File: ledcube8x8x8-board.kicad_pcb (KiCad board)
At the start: 4 copper layers, 120 x 90 mm, 219 parts, among them J1 282836-2, J10 molex_53261-0871, J11 104031-0811, J12 30306-6002HB, J13 hedear, J14 hedear, J15 30306-6002HB, J16 61201021621, J2 molex_53261-0871, J3 molex_53261-0871, J4 molex_53261-0871, J5 molex_53261-0871, J6 molex_53261-0871, J7 molex_53261-0871, J8 molex_53261-0871, J9 molex_53261-0871, Q1 Q_NMOS_GDSD, Q2 Q_NMOS_GDSD, Q3 Q_NMOS_GDSD, Q4 Q_NMOS_GDSD, Q5 Q_NMOS_GDSD, Q6 Q_NMOS_GDSD, Q7 Q_NMOS_GDSD, Q8 Q_NMOS_GDSD, Q9 Q_PMOS_GSD, U1 LM1085IS-12, U10 TL3305AF260QG, U11 IP4220CZ6, U12 IP4220CZ6, U13 XC9572XL-VQ64, U14 SN74LVCC3245APWR, U15 SN74LVCC3245APWR, U16 TS3A27518EPW, U2 STP08CP05MTR, U3 STP08CP05MTR, U4 STP08CP05MTR, U5 STP08CP05MTR, U6 STP08CP05MTR, U7 STP08CP05MTR, U8 STP08CP05MTR, U9 STP08CP05MTR, X1 ASE-40MHz, X2 ASE-25MHz

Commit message: Place whole PS part. Start with PL one.
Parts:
- removed C18, C19: 10nF, Capacitor_SMD:C_0805_2012Metric_Pad1.18x1.45mm_HandSolder
- removed X1: ASE-40MHz, Oscillator:Oscillator_SMD_Abracon_ASE-4Pin_3.2x2.5mm
- removed X2: ASE-25MHz, Oscillator:Oscillator_SMD_Abracon_ASE-4Pin_3.2x2.5mm
- added Q10: Q_PMOS_GSD, Package_TO_SOT_SMD:SOT-23, B.Cu at (52.8, 36.2)
- added R126: 10K, Resistor_SMD:R_0805_2012Metric_Pad1.20x1.40mm_HandSolder, B.Cu at (56.2, 36.2)
- C17, C32, C33, C34, D6, R1, R107, R112, R116, R119, R120, R121, R122, R2, R3, R81, R82, R85, R87, R92, R93, U14, U16: moved to B.Cu
- moved R6 240.0 mm to (153.8, 77.0), turned to 0 degrees
- moved R5 233.5 mm to (143.2, 83.5), turned to 0 degrees
- moved R8 230.9 mm to (153.8, 74.5), turned to 0 degrees
- moved R7 227.5 mm to (131.8, 83.8), turned to 0 degrees
- moved R10 221.8 mm to (153.8, 72.0), turned to 0 degrees
- moved R9 220.1 mm to (150.8, 63.8), turned to 0 degrees
- moved R12 212.7 mm to (153.8, 69.2), turned to 0 degrees
- moved C23 208.5 mm to (35.0, 57.2)
- moved R11 205.8 mm to (150.8, 61.0), turned to 0 degrees
- moved C24 201.3 mm to (30.2, 57.2), turned to 180 degrees
- moved U14 197.3 mm to (34.2, 56.8), turned to 270 degrees
- moved U15 196.9 mm to (33.0, 50.2), turned to 180 degrees
- moved R125 191.8 mm to (71.0, 68.2), turned to 90 degrees
- moved Q9 170.4 mm to (153.1, 44.7)
- moved R123 170.4 mm to (153.0, 40.8)
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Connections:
- C17 pad 1: Net-(C17-Pad1) -> /ps.sch/ESP_PU
- MOD1 pad 3: Net-(C17-Pad1) -> /ps.sch/ESP_PU
- R107 pad 2: Net-(C17-Pad1) -> /ps.sch/ESP_PU
- U16 pad 20: /power_supply.sch/~SYS_RST -> Net-(Q10-Pad3)
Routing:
- net ESP_3V3: track 0.00 -> 201.2 mm, vias 0 -> 8
- net GNDD: track 57.4 -> 128.6 mm
- net GND: track 56.6 -> 113.0 mm
- net /DATA_LED1: track 0.00 -> 55.5 mm, vias 0 -> 3
- net /ps.sch/TDI: track 0.00 -> 54.6 mm, vias 0 -> 2
- net /ps.sch/SDDATA1: track 0.00 -> 54.2 mm
- net /pl.sch/LED_R: track 0.00 -> 54.2 mm, vias 0 -> 1
- net /ps.sch/TMS: track 0.00 -> 51.7 mm, vias 0 -> 1
- net /pl.sch/LED_G: track 0.00 -> 50.7 mm, vias 0 -> 1
- net /ps.sch/TCK: track 0.00 -> 47.9 mm, vias 0 -> 3
- net /ps.sch/SDDATA0: track 0.00 -> 47.8 mm
- net /pl.sch/LED_O1: track 0.00 -> 46.4 mm, vias 0 -> 1
- net /ps.sch/TDO: track 0.00 -> 45.5 mm, vias 0 -> 4
- net /pl.sch/LED_O2: track 0.00 -> 41.9 mm, vias 0 -> 1
- net /ps.sch/SD_CD: track 0.00 -> 39.6 mm, vias 0 -> 2
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- added copper zone on In1.Cu, net GND
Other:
- board size 120 x 90 mm -> 112.5 x 79.2 mm

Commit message: PCB: Re-work routing of led multiplexer part
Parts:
- added C18: 10nF, Capacitor_SMD:C_0805_2012Metric_Pad1.18x1.45mm_HandSolder, F.Cu at (131.4, 28.5)
- added C19: 10nF, Capacitor_SMD:C_0805_2012Metric_Pad1.18x1.45mm_HandSolder, F.Cu at (136.2, 28.5)
- added X1: ASE-40MHz, Oscillator:Oscillator_SMD_Abracon_ASE-4Pin_3.2x2.5mm, F.Cu at (131.5, 24.7)
- added X2: ASE-25MHz, Oscillator:Oscillator_SMD_Abracon_ASE-4Pin_3.2x2.5mm, F.Cu at (136.6, 24.7)
- C21, C22, R125: moved to B.Cu
- moved NT2 115.5 mm to (33.0, 56.2)
- moved C22 99.5 mm to (31.5, 45.0), turned to 180 degrees
- moved U13 99.1 mm to (142.2, 2.00)
- moved C21 94.3 mm to (36.2, 45.0)
- moved R125 76.0 mm to (143.8, 46.2), turned to 0 degrees
- moved J12 75.8 mm to (146.2, 51.8), turned to 270 degrees
- moved NT1 53.9 mm to (104.0, 66.5)
- moved J2 52.4 mm to (202.5, 89.5)
- moved Q1 52.4 mm to (190.8, 94.2)
- moved Q2 52.4 mm to (190.8, 94.2)
- moved Q3 52.4 mm to (179.2, 94.2)
- moved Q4 52.4 mm to (179.2, 94.2)
- moved Q5 52.4 mm to (190.8, 84.5)
- moved Q6 52.4 mm to (190.8, 84.5)
- moved Q7 52.4 mm to (179.2, 84.5)
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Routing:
- net GND: track 113.0 -> 463.3 mm, vias 0 -> 42
- net /pl.sch/VCC_5V0: track 58.0 -> 267.8 mm, vias 1 -> 18
- net ESP_3V3: track 201.2 -> 5.00 mm, vias 8 -> 0
- net /ps.sch/TDI: track 54.6 -> 0.00 mm, vias 2 -> 0
- net /ps.sch/SDDATA1: track 54.2 -> 0.00 mm
- net /pl.sch/LED_R: track 54.2 -> 0.00 mm, vias 1 -> 0
- net /ps.sch/TMS: track 51.7 -> 0.00 mm, vias 1 -> 0
- net /pl.sch/LED_G: track 50.7 -> 0.00 mm, vias 1 -> 0
- net /ps.sch/TCK: track 47.9 -> 0.00 mm, vias 3 -> 0
- net /ps.sch/SDDATA0: track 47.8 -> 0.00 mm
- net /pl.sch/LED_O1: track 46.4 -> 0.00 mm, vias 1 -> 0
- net /ps.sch/TDO: track 45.5 -> 0.00 mm, vias 4 -> 0
- net /DATA_LED2: track 21.6 -> 65.4 mm
- net /DATA_LED1: track 55.5 -> 12.3 mm, vias 3 -> 1
- net /pl.sch/LED_O2: track 41.9 -> 0.00 mm, vias 1 -> 0
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- added copper zone on In2.Cu, net /pl.sch/VCC_5V0

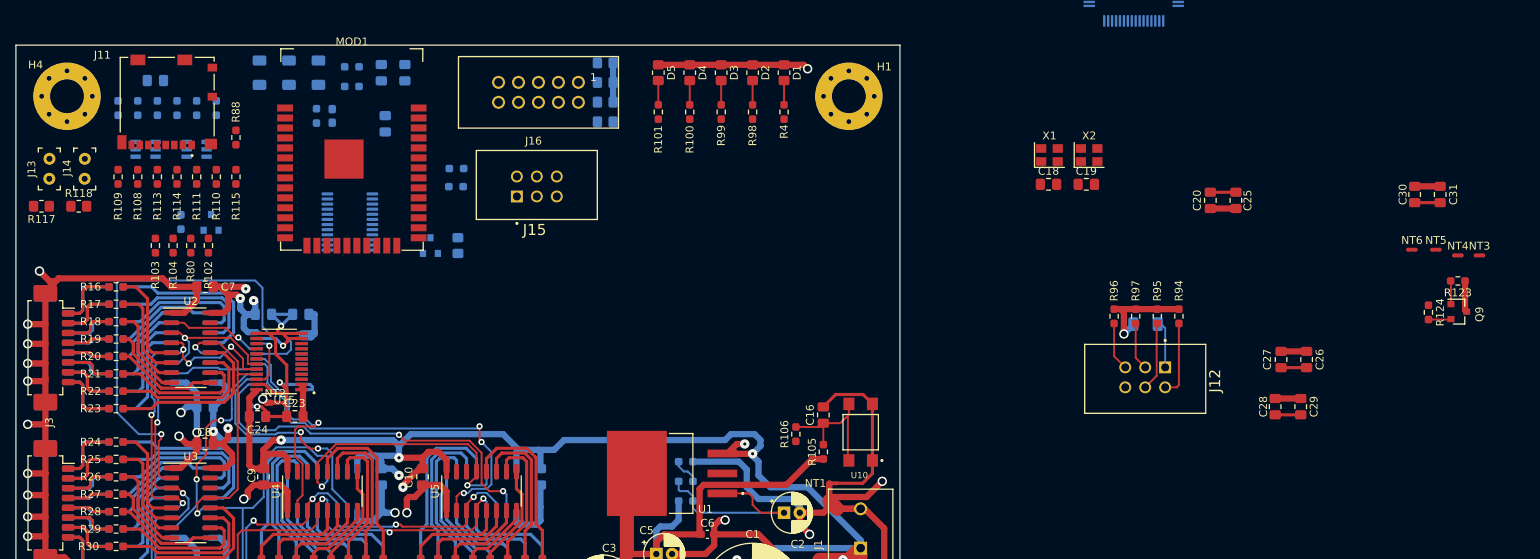
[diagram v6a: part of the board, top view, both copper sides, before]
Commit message: PCB: Re-work routing of PS part (now complete)
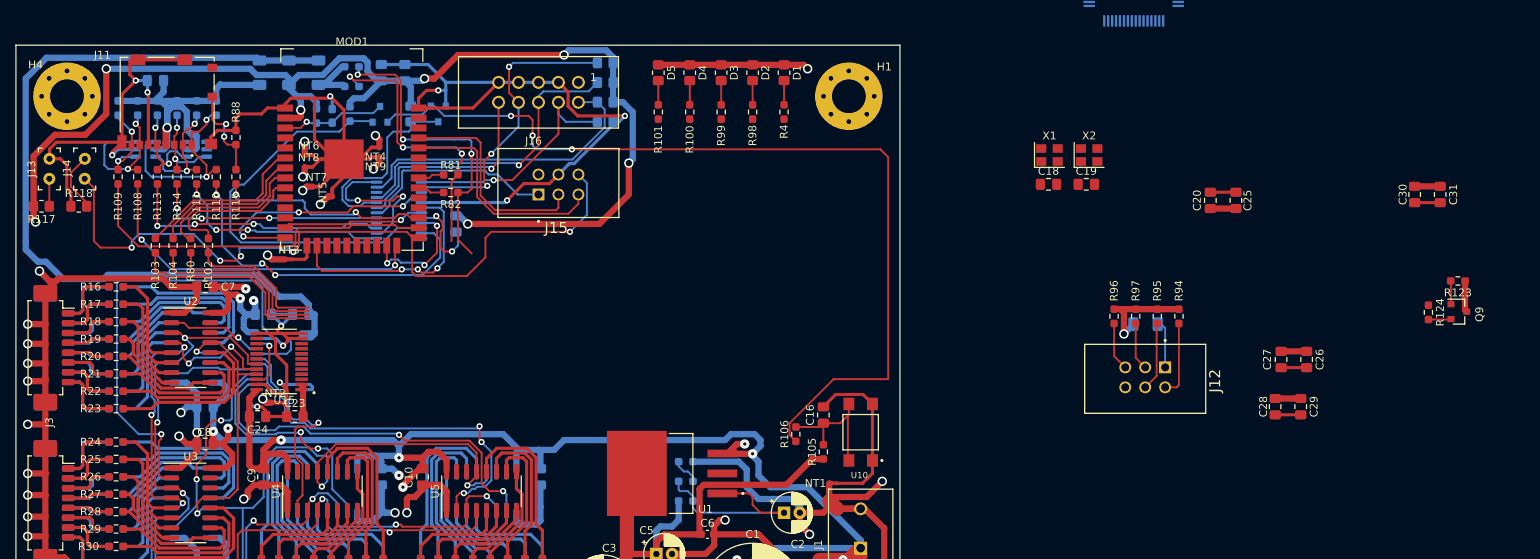
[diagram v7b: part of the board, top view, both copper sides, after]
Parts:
- added NT7: Net-Tie_2, NetTie:NetTie-2_SMD_Pad0.5mm, F.Cu at (38.2, 28.8)
- added NT8: Net-Tie_2, NetTie:NetTie-2_SMD_Pad0.5mm, F.Cu at (37.2, 26.2)
- added NT9: Net-Tie_2, NetTie:NetTie-2_SMD_Pad0.5mm, F.Cu at (45.8, 25.0)
- R81, R82: moved to F.Cu
- moved NT3 151.5 mm to (34.8, 38.0)
- moved NT6 140.9 mm to (37.2, 24.8)
- moved NT5 140.6 mm to (40.2, 29.5), turned to 90 degrees
- moved NT4 138.4 mm to (45.8, 23.8), turned to 180 degrees
- moved D6 25.5 mm to (46.3, 19.5)
- moved R112 25.5 mm to (42.5, 19.5)
- moved R126 17.8 mm to (50.2, 19.5), turned to 90 degrees
- moved Q10 16.8 mm to (53.8, 19.5), turned to 270 degrees
- moved C34 15.6 mm to (56.0, 33.5)
- moved U16 6.43 mm to (48.8, 31.8), turned to 180 degrees
- moved J15 2.76 mm to (66.5, 29.8)
- moved R81 1.09 mm to (55.3, 27.2)
- moved R82 1.00 mm to (55.3, 29.5)
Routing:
- net GNDD: track 88.4 -> 294.7 mm, vias 4 -> 11
- net ESP_3V3: track 5.00 -> 160.3 mm, vias 0 -> 7
- net /power_supply.sch/~SYS_RST: track 0.00 -> 114.9 mm, vias 0 -> 3
- net /pl.sch/VCC_3V3: track 113.7 -> 214.5 mm
- net /ps.sch/GPIO0: track 0.00 -> 94.7 mm, vias 0 -> 5
- net /ps.sch/PRG_REST: track 0.00 -> 52.4 mm
- net /ps.sch/SDDATA1: track 0.00 -> 46.8 mm
- net SD_3V3: track 0.00 -> 45.0 mm, vias 0 -> 1
- net /ps.sch/SDDATA0: track 0.00 -> 43.9 mm, vias 0 -> 2
- net /ps.sch/SD_DAT2: track 0.00 -> 43.6 mm, vias 0 -> 3
- net /pl.sch/I2C_SDA: track 0.00 -> 39.8 mm, vias 0 -> 3
- net /ps.sch/TDO: track 0.00 -> 39.6 mm, vias 0 -> 1
- net /ps.sch/TMS: track 0.00 -> 39.1 mm
- net /ps.sch/TDI: track 0.00 -> 37.5 mm, vias 0 -> 3
- net /pl.sch/I2C_SCL: track 0.00 -> 36.2 mm, vias 0 -> 3
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
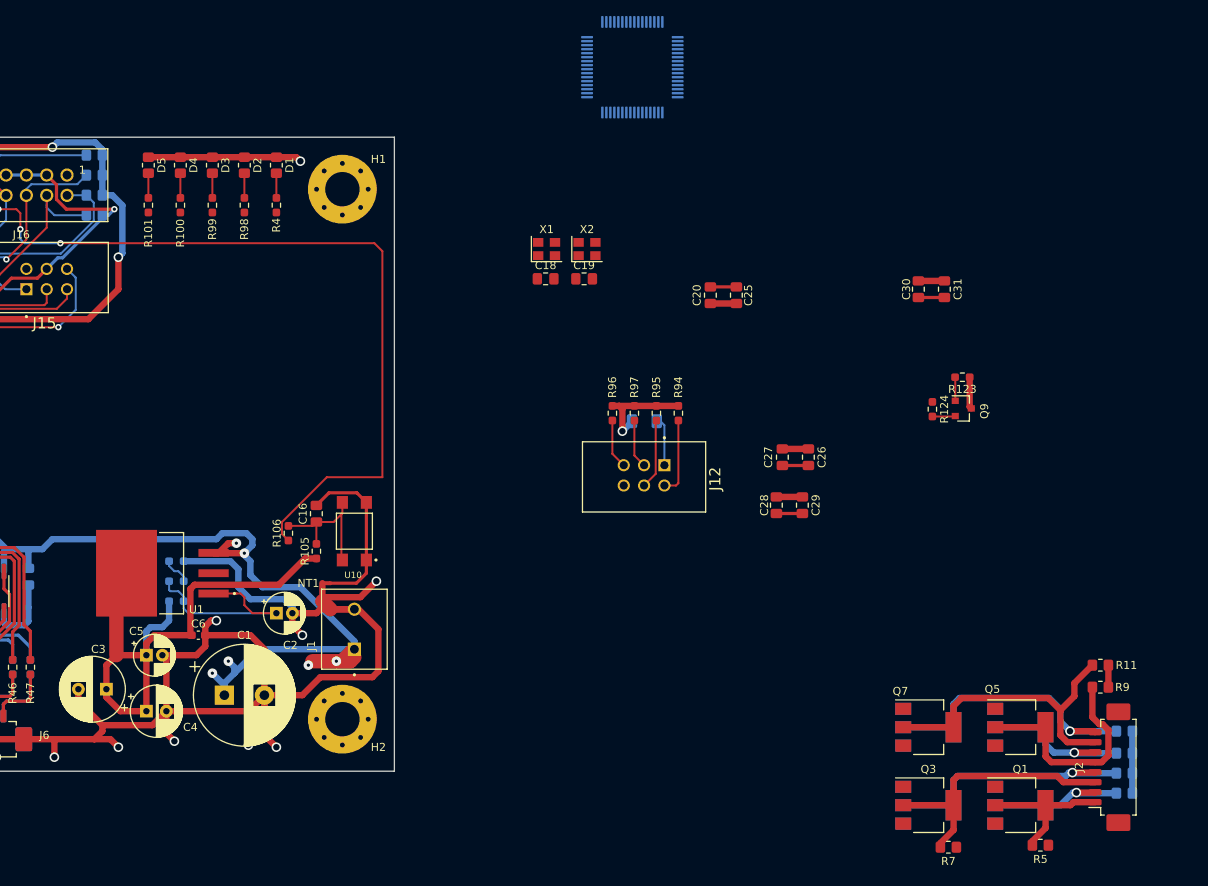
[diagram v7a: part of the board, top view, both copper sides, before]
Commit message: PCB: Place led layer multiplexer
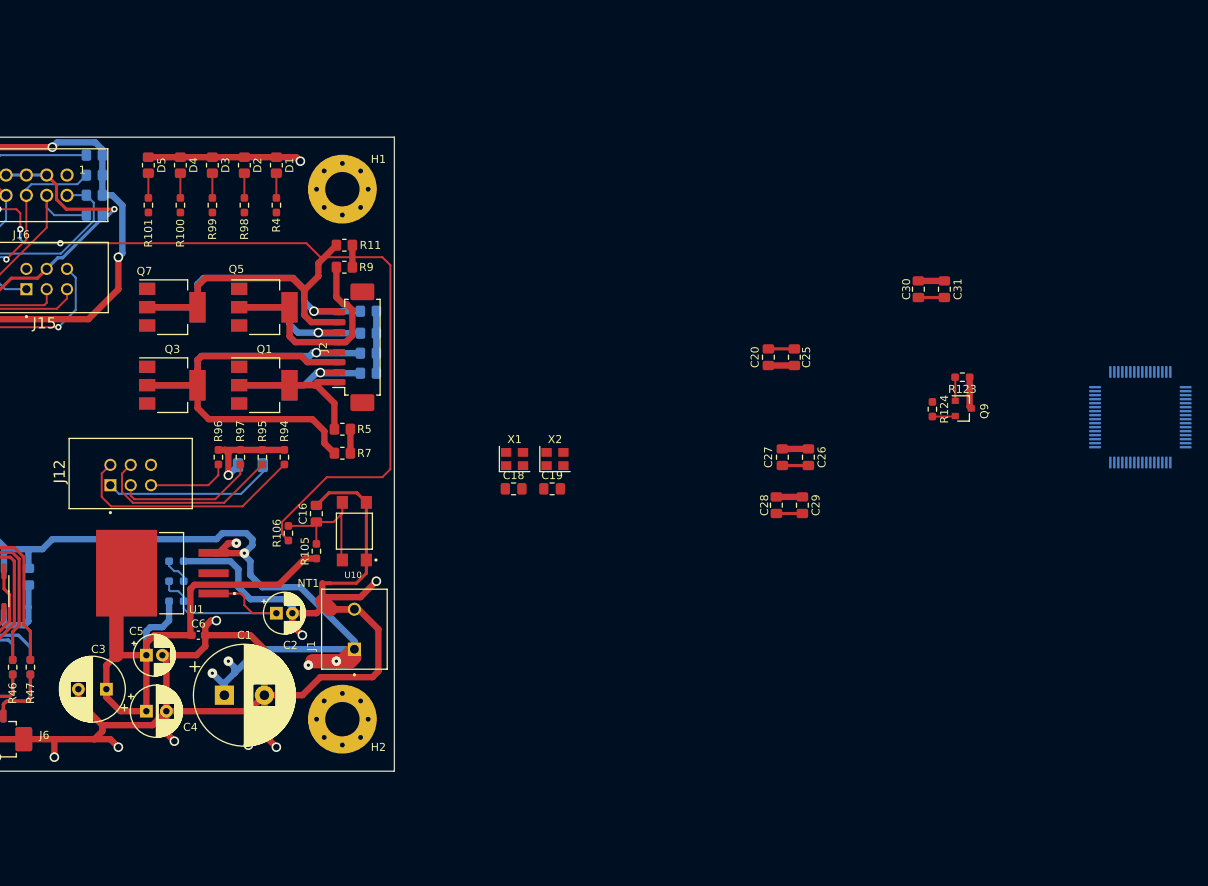
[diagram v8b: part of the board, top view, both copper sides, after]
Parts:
- moved J2 108.1 mm to (108.0, 37.0)
- moved Q1 108.1 mm to (96.2, 41.8)
- moved Q2 108.1 mm to (96.2, 41.8)
- moved Q3 108.1 mm to (84.8, 41.8)
- moved Q4 108.1 mm to (84.8, 41.8)
- moved Q5 108.1 mm to (96.2, 32.0)
- moved Q6 108.1 mm to (96.2, 32.0)
- moved Q7 108.1 mm to (84.8, 32.0)
- moved Q8 108.1 mm to (84.8, 32.0)
- moved R10 108.1 mm to (109.2, 35.2)
- moved R11 108.1 mm to (106.2, 24.2)
- moved R12 108.1 mm to (109.2, 32.5)
- moved R6 108.1 mm to (109.2, 40.2)
- moved R8 108.1 mm to (109.2, 37.8)
- moved R9 108.1 mm to (106.2, 27.0)
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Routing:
- net /pl.sch/TDI: track 9.71 -> 29.9 mm
- net /layer_selector.sch/LAYER_SEL3: track 33.6 -> 50.8 mm
- net Net-(J12-Pad1): track 6.16 -> 21.5 mm
- net /pl.sch/TMS: track 8.77 -> 23.9 mm
- net /pl.sch/TCK: track 6.09 -> 17.7 mm
- net /pl.sch/TDO: track 6.18 -> 10.3 mm
- net /pl.sch/VCC_5V0: track 267.8 -> 270.8 mm
- net /layer_selector.sch/LAYER_SEL1: track 18.3 -> 19.3 mm
